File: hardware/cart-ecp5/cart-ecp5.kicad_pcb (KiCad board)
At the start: 4 copper layers, 100 x 60 mm, 120 parts, among them J1 JTAG, J2 MicroSD_Molex_1040310811, J3 N64_Cartridge_Bus, J5 USB_C_USB2.0, U1 LFE5U-25F-xBG256x, U10 93C46BT-I_OT, U11 FT2232HQ, U2 W25Q128JVSIM, U3 S27KS0641, U4 ATtiny25-20SU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

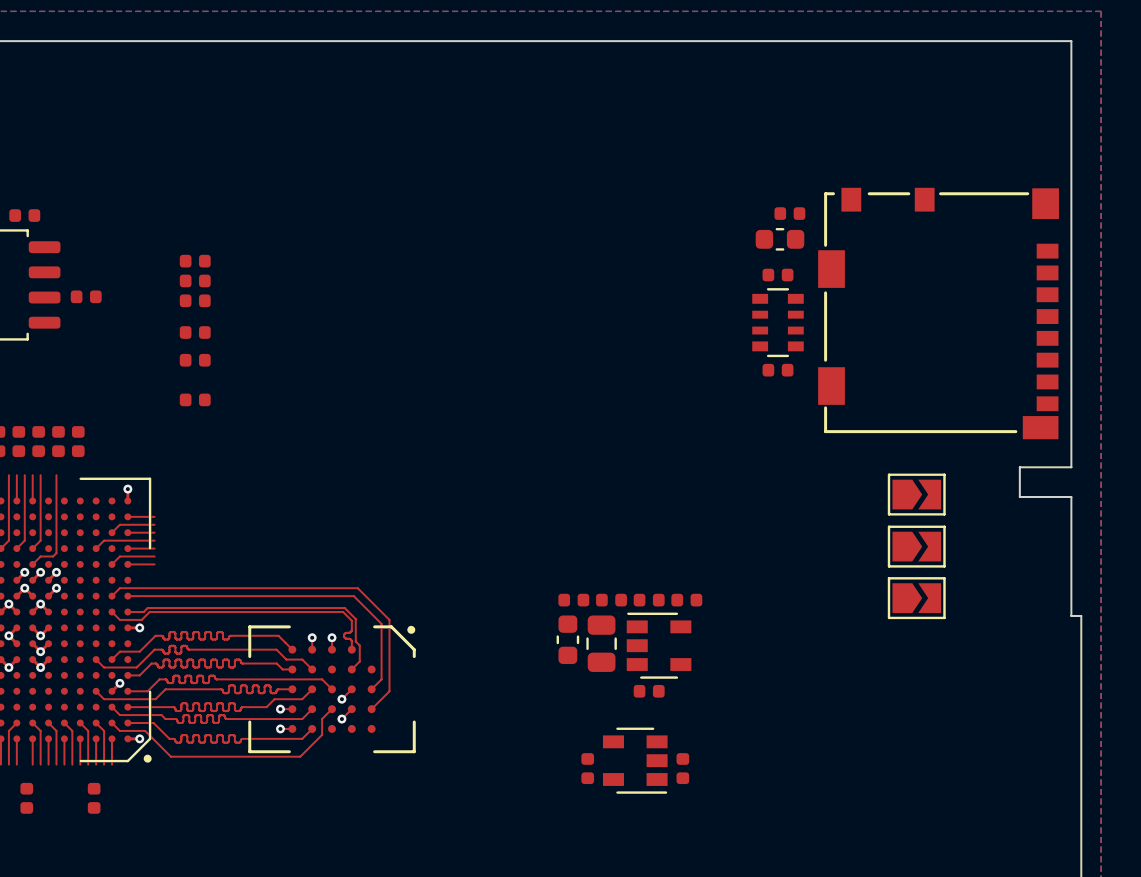
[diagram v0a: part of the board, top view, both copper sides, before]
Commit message: Adjust MicroSD pullup resistor placement
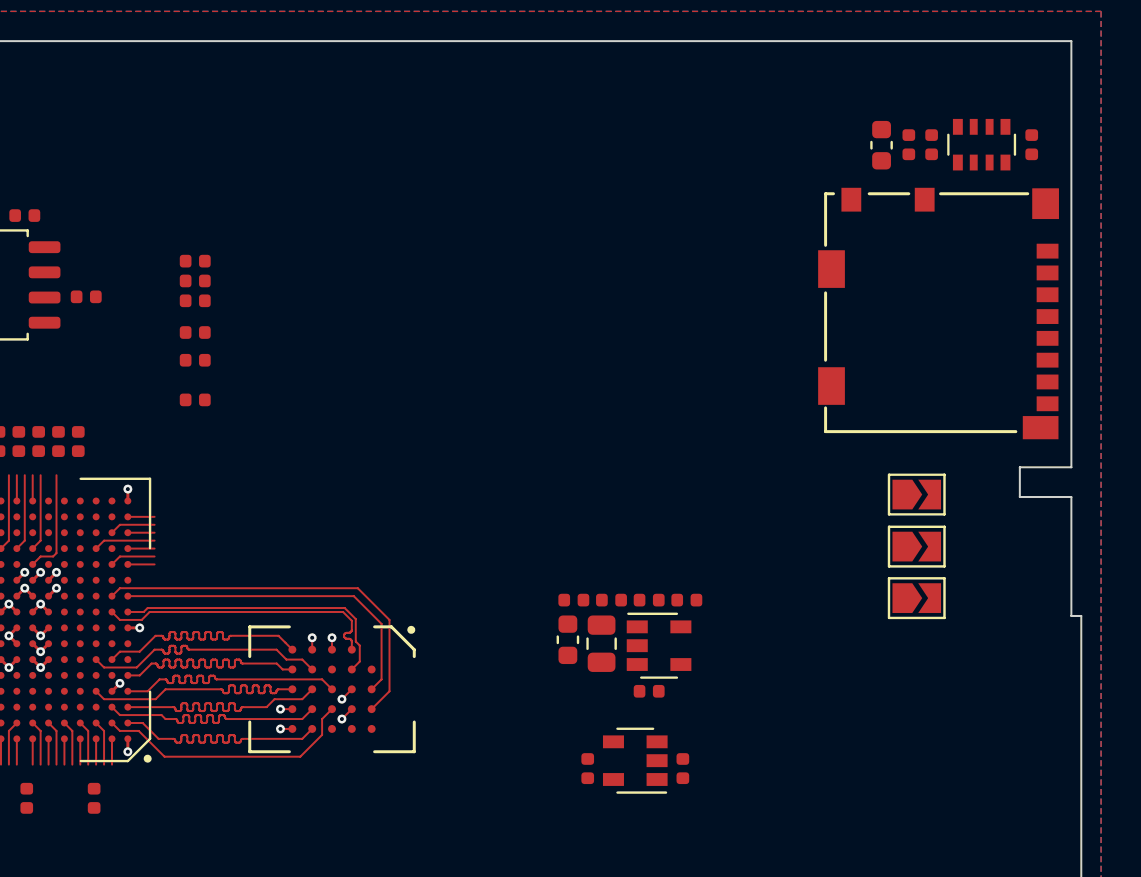
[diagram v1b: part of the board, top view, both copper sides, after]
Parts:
- moved R5 17.1 mm to (197.5, 79.2), turned to 270 degrees
- moved RN7 13.6 mm to (195.0, 79.2), turned to 90 degrees
- moved R4 10.2 mm to (192.4, 79.2), turned to 270 degrees
- moved C3 6.99 mm to (189.9, 79.2), turned to 90 degrees
- moved C4 6.93 mm to (191.3, 79.2), turned to 90 degrees

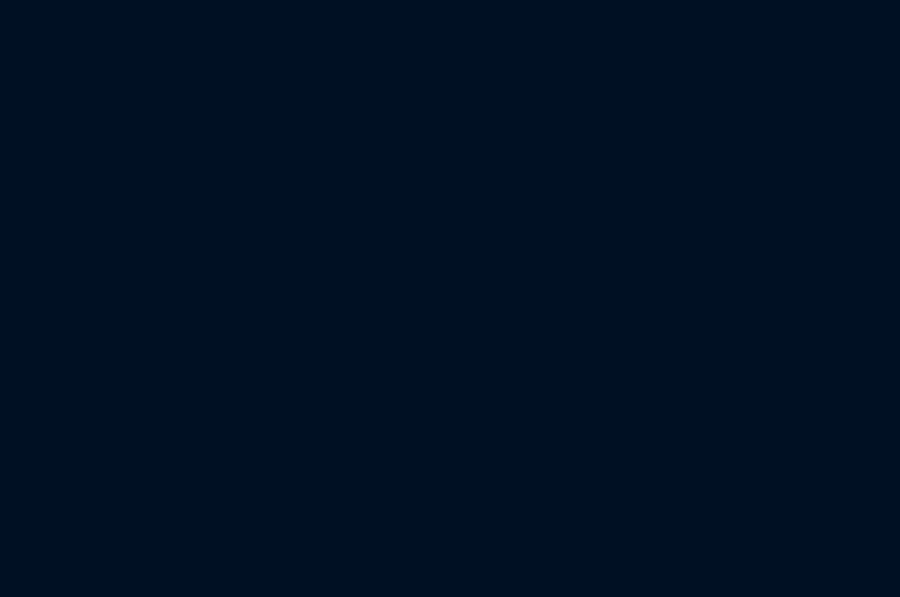
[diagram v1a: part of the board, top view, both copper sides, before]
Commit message: Preliminary placement of TPS2121 and supporting passives
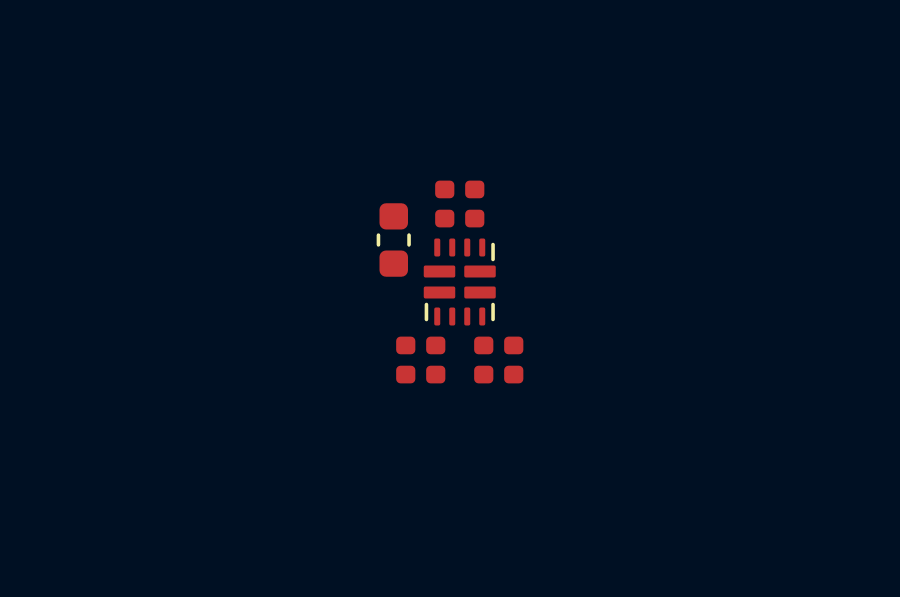
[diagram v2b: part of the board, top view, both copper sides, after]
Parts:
- added C63: 10u, Capacitor_SMD:C_0603_1608Metric, F.Cu at (170.6, 59.5)
- added C64: 10n, Capacitor_SMD:C_0402_1005Metric, F.Cu at (172.3, 58.3)
- added R25: 23k7, Resistor_SMD:R_0402_1005Metric, F.Cu at (174.6, 63.5)
- added R26: 5k1, Resistor_SMD:R_0402_1005Metric, F.Cu at (173.6, 63.5)
- added R27: 23k7, Resistor_SMD:R_0402_1005Metric, F.Cu at (171.0, 63.5)
- added R28: 5k1, Resistor_SMD:R_0402_1005Metric, F.Cu at (172.0, 63.5)
- added R29: 47k, Resistor_SMD:R_0402_1005Metric, F.Cu at (173.3, 58.3)
- added U12: TPS2121, ng_package_qfn:Texas_VQFN-HR-12, F.Cu at (172.8, 60.9)
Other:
- rule pad_to_mask_clearance: 0.13 -> 0.05

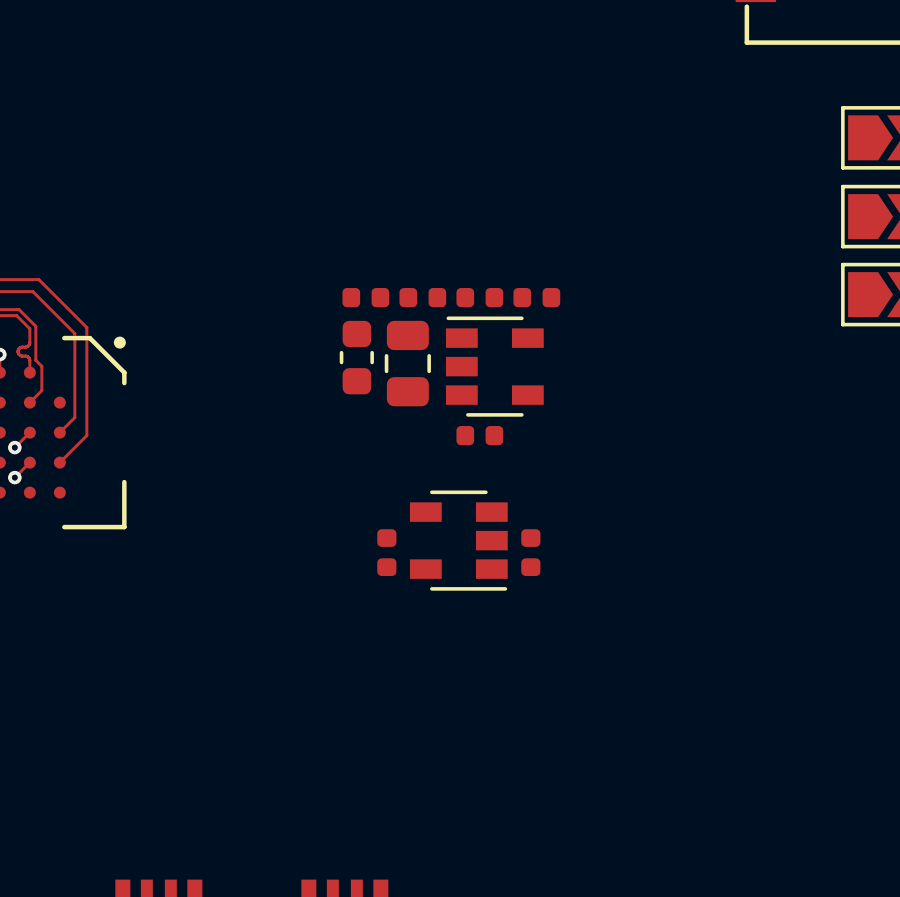
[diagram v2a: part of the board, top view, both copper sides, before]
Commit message: Add a switching supply for a 1V8 rail
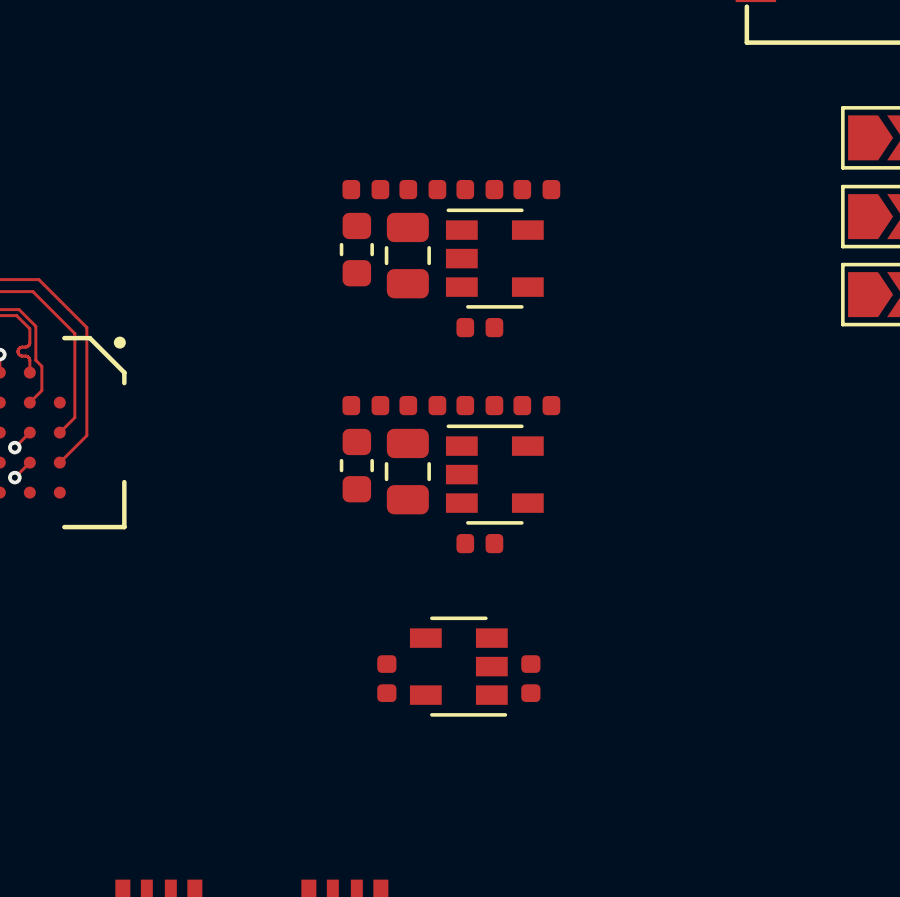
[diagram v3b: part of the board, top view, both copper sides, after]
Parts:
- added C65: 4u7, Capacitor_SMD:C_0402_1005Metric, F.Cu at (178.2, 110.4)
- added C66: 6p8, Capacitor_SMD:C_0402_1005Metric, F.Cu at (176.3, 105.8)
- added C67: 10u, Capacitor_SMD:C_0603_1608Metric, F.Cu at (174.1, 107.8)
- added C68: 1u, Capacitor_SMD:C_0402_1005Metric, F.Cu at (174.4, 105.8)
- added L3: 2u2, Inductor_SMD:L_0805_2012Metric, F.Cu at (175.8, 108.0)
- added R30: R, Resistor_SMD:R_0402_1005Metric, F.Cu at (178.2, 105.8)
- added R31: 100k, Resistor_SMD:R_0402_1005Metric, F.Cu at (180.1, 105.8)
- added U13: TLV62568DBV, Package_TO_SOT_SMD:SOT-23-5, F.Cu at (178.7, 108.1)
- moved C12 4.20 mm to (179.9, 114.9)
- moved C13 4.20 mm to (175.1, 114.9)
- moved U8 4.20 mm to (177.5, 114.5)
- moved C15 3.60 mm to (176.3, 98.6)
- moved C17 3.60 mm to (174.1, 100.6)
- moved C19 3.60 mm to (174.4, 98.6)
- moved L2 3.60 mm to (175.8, 100.8)
- moved R12 3.60 mm to (178.2, 98.6)
- moved R13 3.60 mm to (180.1, 98.6)
- moved C11 3.60 mm to (178.2, 103.2)
- moved U7 3.60 mm to (178.7, 100.9)

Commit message: Use 1V8 for HyperRAM interface
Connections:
- C55 pad 1: P3V3 -> P1V8
- C62 pad 1: P3V3 -> P1V8
- U1 pad H6: P3V3 -> P1V8
- U1 pad H7: P3V3 -> P1V8
- U3 pad B4: P3V3 -> P1V8
- U3 pad D1: P3V3 -> P1V8
- U3 pad E4: P3V3 -> P1V8
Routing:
- net P1V8: track 0.00 -> 3.04 mm, vias 0 -> 4
- net P3V3: track 9.83 -> 6.79 mm, vias 11 -> 7

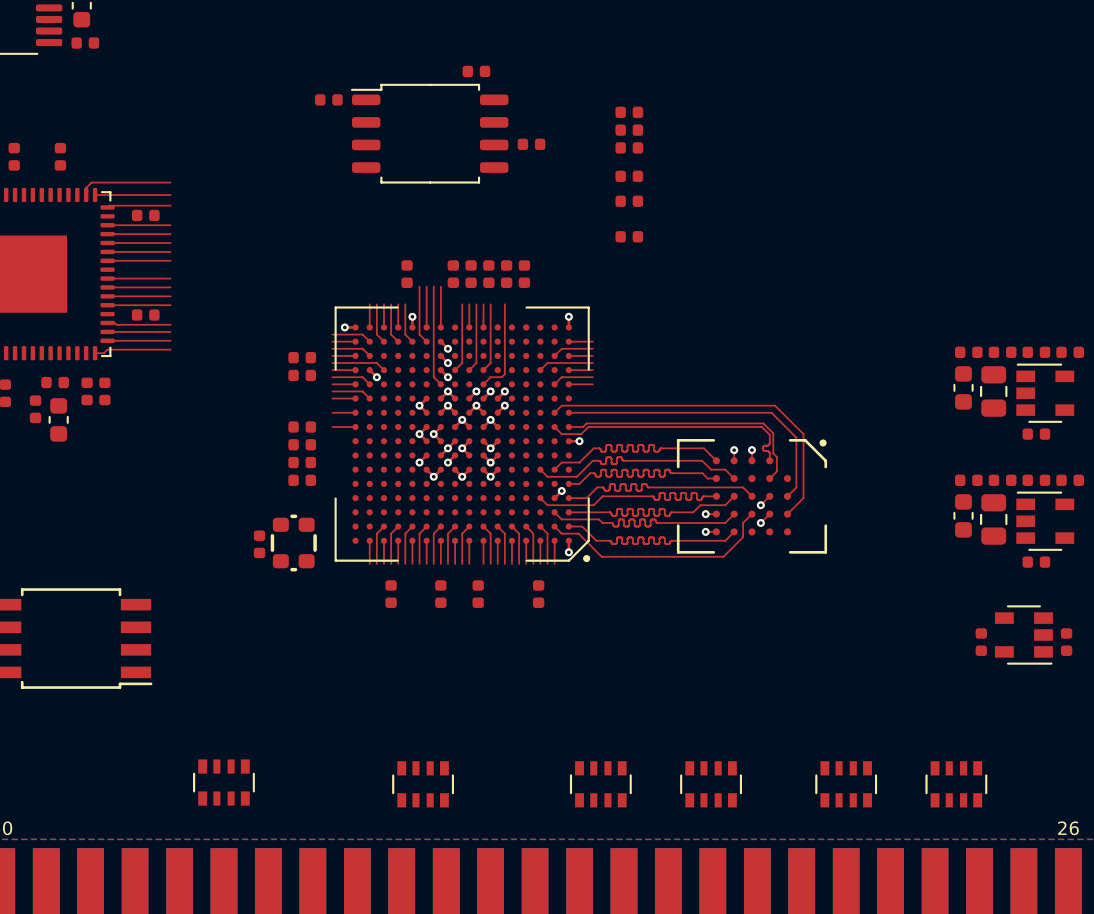
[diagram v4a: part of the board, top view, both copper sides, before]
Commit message: Place bypass caps along right side of FPGA and optimize power island
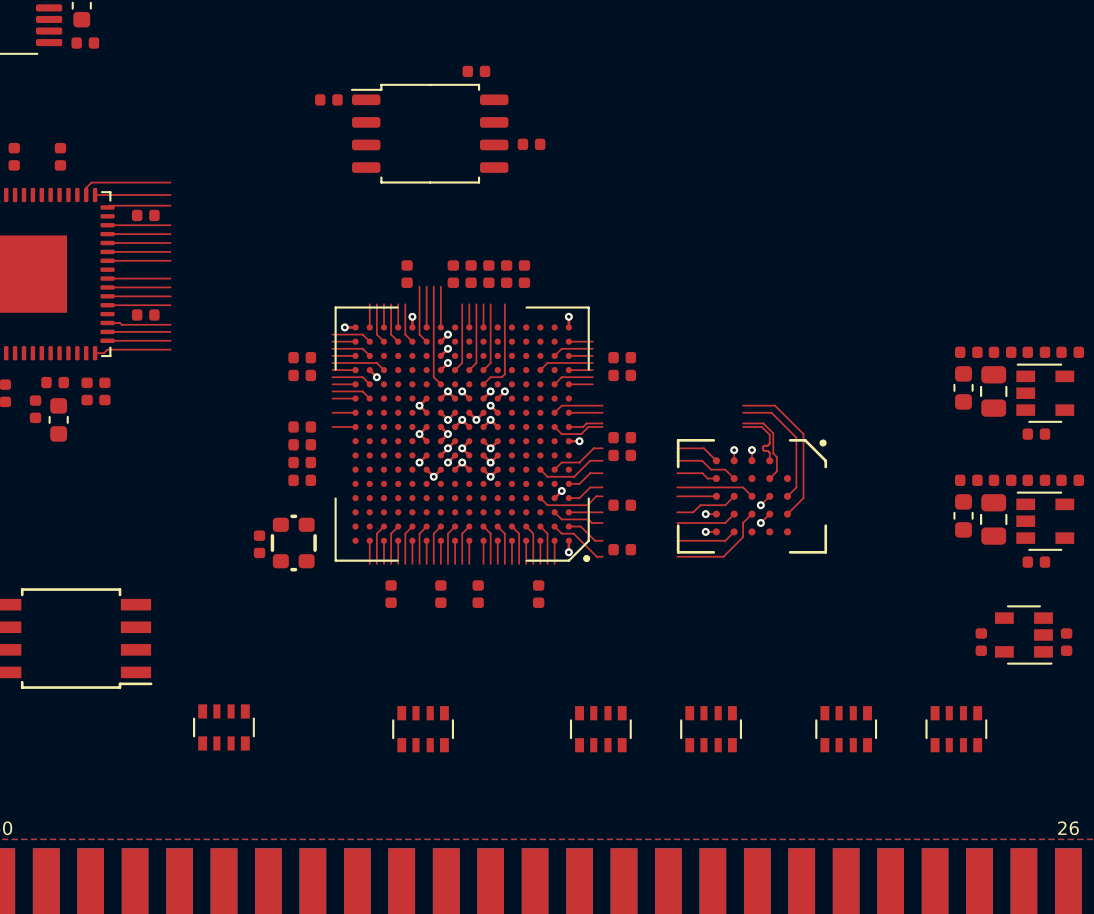
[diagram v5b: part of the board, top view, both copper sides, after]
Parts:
- moved C62 17.6 mm to (154.9, 109.7)
- moved C55 17.1 mm to (154.9, 107.2)
- moved C43 16.3 mm to (154.9, 103.4)
- moved C42 15.7 mm to (154.9, 104.4)
- moved C54 13.8 mm to (154.9, 99.9)
- moved C61 13.8 mm to (154.9, 98.9)
- moved RN1 3.10 mm to (173.7, 119.8)
- moved RN2 3.10 mm to (167.5, 119.8)
- moved RN3 3.10 mm to (159.9, 119.8)
- moved RN4 3.10 mm to (153.7, 119.8)
- moved RN5 3.10 mm to (143.7, 119.8)
- moved RN6 3.10 mm to (132.5, 119.7)
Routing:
- net HRAM_DQ6: track 13.0 -> 4.47 mm
- net HRAM_RESET_B: track 19.7 -> 11.8 mm
- net HRAM_CS_B: track 16.9 -> 8.99 mm
- net HRAM_CK_P: track 14.6 -> 6.70 mm
- net HRAM_CK_N: track 14.6 -> 6.70 mm
- net HRAM_DQ0: track 13.0 -> 5.47 mm
- net HRAM_DQ4: track 13.0 -> 5.64 mm
- net HRAM_DQ7: track 13.1 -> 5.69 mm
- net HRAM_DQ5: track 13.0 -> 6.07 mm
- net HRAM_DQ3: track 13.0 -> 6.36 mm
- net HRAM_RWDS: track 13.0 -> 6.56 mm
- net HRAM_DQ1: track 13.0 -> 7.65 mm
- net HRAM_DQ2: track 13.3 -> 9.07 mm

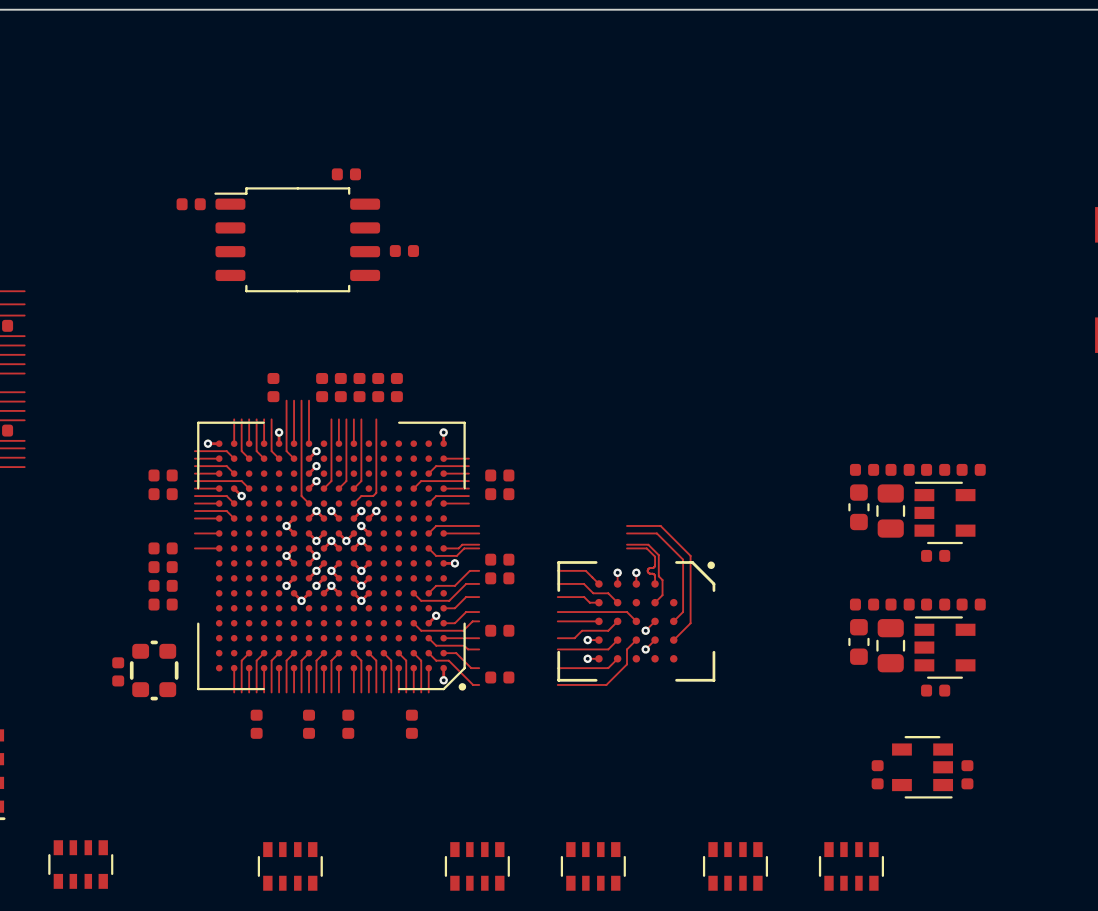
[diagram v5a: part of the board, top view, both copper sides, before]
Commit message: Tweak the top edge of the FPGA
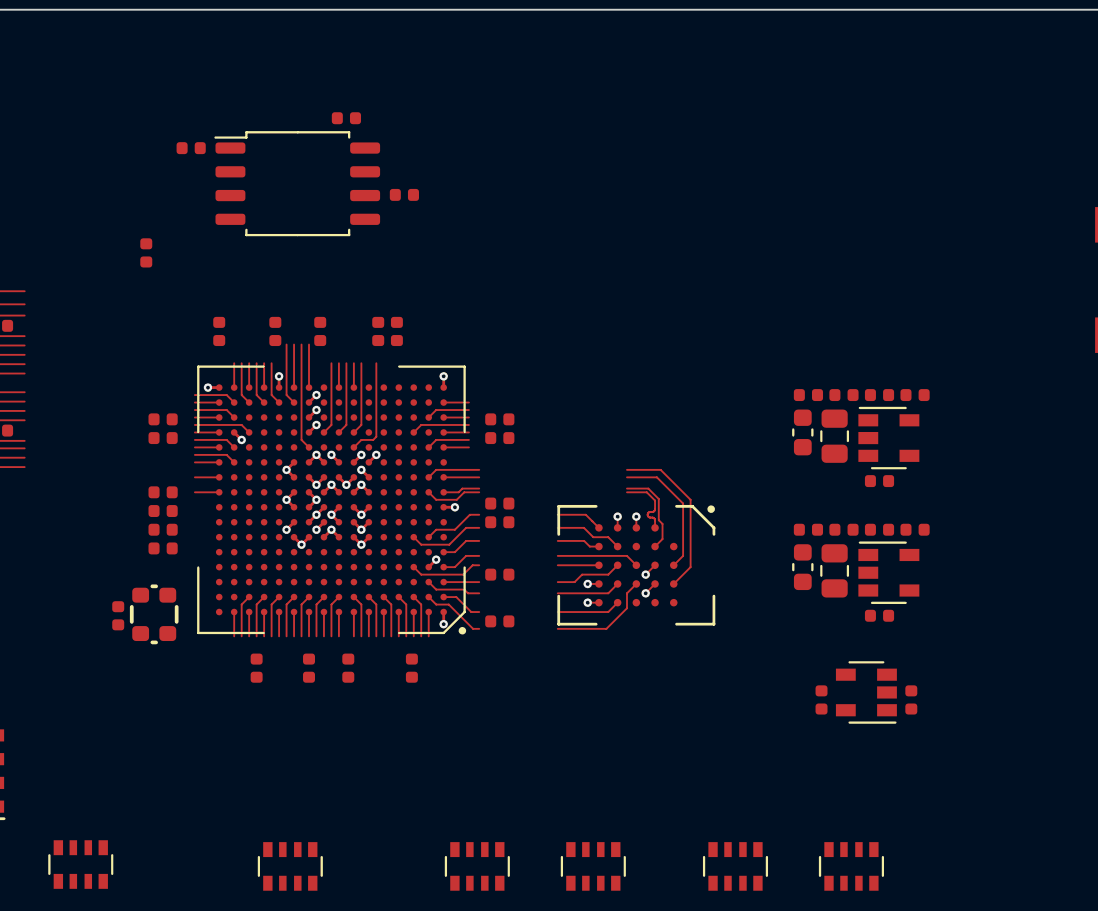
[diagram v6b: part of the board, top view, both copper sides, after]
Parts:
- moved R3 9.90 mm to (136.0, 87.0)
- moved C48 6.26 mm to (139.9, 91.2)
- moved C11 5.00 mm to (175.2, 99.2)
- moved C12 5.00 mm to (176.9, 110.9)
- moved C13 5.00 mm to (172.1, 110.9)
- moved C15 5.00 mm to (173.3, 94.6)
- moved C17 5.00 mm to (171.1, 96.6)
- moved C19 5.00 mm to (171.4, 94.6)
- moved C65 5.00 mm to (175.2, 106.4)
- moved C66 5.00 mm to (173.3, 101.8)
- moved C67 5.00 mm to (171.1, 103.8)
- moved C68 5.00 mm to (171.4, 101.8)
- moved L2 5.00 mm to (172.8, 96.8)
- moved L3 5.00 mm to (172.8, 104.0)
- moved R12 5.00 mm to (175.2, 94.6)
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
